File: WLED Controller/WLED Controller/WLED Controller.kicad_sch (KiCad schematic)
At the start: 1 part, among them U1 ESP32-WROOM-32

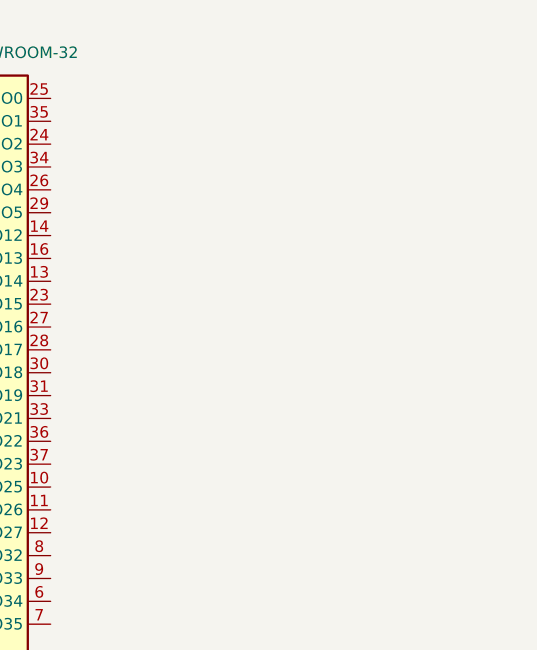
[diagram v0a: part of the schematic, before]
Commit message: Added Level Shifter
SN74AHCT125N
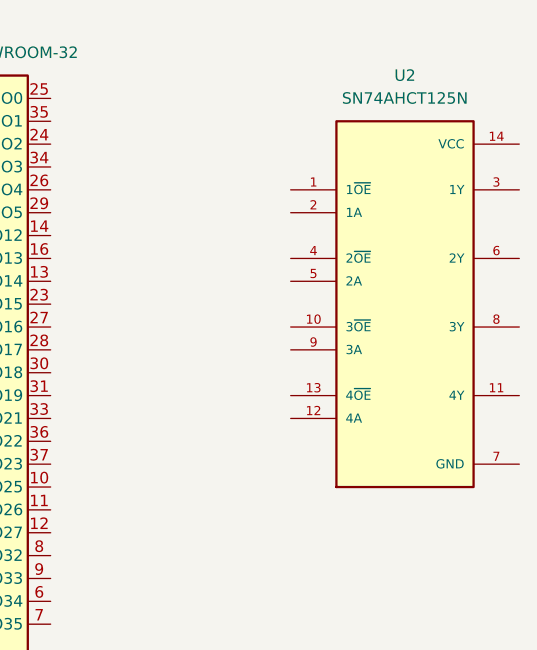
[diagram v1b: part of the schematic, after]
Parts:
- added U2: SN74AHCT125N, Level Shifters:SN74AHCT125N, symbol SN74AHCT125N:SN74AHCT125N
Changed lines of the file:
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@@
+	)
+	(symbol
+		(lib_id "SN74AHCT125N:SN74AHCT125N")
+		(at 166.37 64.77 0)
+		(unit 1)
+		(exclude_from_sim no)
+		(in_bom yes)
+		(on_board yes)
+		(dnp no)
+		(fields_autoplaced yes)
+		(property "Reference" "U2"
+			(at 166.37 39.37 0)
+			(effects
+				(font
+					(size 1.27 1.27)
+				)
+			)
+		)
+		(property "Value" "SN74AHCT125N"
+			(at 166.37 41.91 0)
+			(effects
+				(font
+					(size 1.27 1.27)
+				)
+			)
+		)
+		(property "Footprint" "Level Shifters:SN74AHCT125N"
+			(at 166.37 64.77 0)
+			(effects
+				(font
+					(size 1.27 1.27)
+				)
+				(justify bottom)
+				(hide yes)
+			)
+		)
+		(property "Datasheet" ""
+			(at 166.37 64.77 0)
+			(effects
+				(font
+					(size 1.27 1.27)
+				)
+				(hide yes)
+			)
+		)
+		(property "Description" ""
+			(at 166.37 64.77 0)
+			(effects
+				(font
+					(size 1.27 1.27)
+				)
+				(hide yes)
+			)
+		)
+		(property "PARTREV" "Q"
+			(at 166.37 64.77 0)
+			(effects
+				(font
+					(size 1.27 1.27)
+				)
+				(justify bottom)
+				(hide yes)
+			)
+		)
+		(property "STANDARD" "Manufacturer Recommendations"
+			(at 166.37 64.77 0)
+			(effects
+				(font
+					(size 1.27 1.27)
+				)
+				(justify bottom)
+				(hide yes)
+			)
+		)
+		(property "MAXIMUM_PACKAGE_HEIGHT" "5.08mm"
+			(at 166.37 64.77 0)
+			(effects
+				(font
+					(size 1.27 1.27)
+				)
+				(justify bottom)
+				(hide yes)
+			)
+		)
+		(property "MANUFACTURER" "Texas Instruments"
+			(at 166.37 64.77 0)
+			(effects
+				(font
+					(size 1.27 1.27)
+				)
+				(justify bottom)
+				(hide yes)
+			)
+		)
+		(pin "1"
+		)
+		(pin "5"
+		)
+		(pin "12"
+		)
+		(pin "9"
+		)
+		(pin "8"
+		)
+		(pin "3"
+		)
+		(pin "11"
+		)
+		(pin "7"
+		)
+		(pin "4"
+		)
+		(pin "14"
+		)
+		(pin "13"
+		)
+		(pin "6"
+		)
+		(pin "2"
+		)
+		(pin "10"
+		)
+		(instances
+			(project ""
+				(path "/e8736a94-4ef8-408c-b7cc-dcf1b7df2117"
+					(reference "U2")
+					(unit 1)
+				)
+			)
+		)
 	)
 	(symbol

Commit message: Audio Jack Added
Added Audio Jack
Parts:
- added J1: AudioJack3, Connector_Audio:Jack_3.5mm_CUI_SJ-3523-SMT_Horizontal, symbol Connector_Audio:AudioJack3
- added J2: AudioJack4, Connector_Audio:Jack_3.5mm_PJ320D_Horizontal, symbol Connector_Audio:AudioJack4
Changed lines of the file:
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@@
+	)
+	(symbol
+		(lib_id "Connector_Audio:AudioJack4")
+		(at 218.44 55.88 0)
+		(unit 1)
+		(exclude_from_sim no)
+		(in_bom yes)
+		(on_board yes)
+		(dnp no)
+		(fields_autoplaced yes)
+		(property "Reference" "J2"
+			(at 215.9 46.99 0)
+			(effects
+				(font
+					(size 1.27 1.27)
+				)
+			)
+		)
+		(property "Value" "AudioJack4"
+			(at 215.9 49.53 0)
+			(effects
+				(font
+					(size 1.27 1.27)
+				)
+			)
+		)
+		(property "Footprint" "Connector_Audio:Jack_3.5mm_PJ320D_Horizontal"
+			(at 218.44 55.88 0)
+			(effects
+				(font
+					(size 1.27 1.27)
+				)
+				(hide yes)
+			)
+		)
+		(property "Datasheet" "https://sharvielectronics.com/wp-content/uploads/2021/07/Audio-Jack-3.5mm-TRRS-SMD.pdf"
+			(at 218.44 55.88 0)
+			(effects
+				(font
+					(size 1.27 1.27)
+				)
+				(hide yes)
+			)
+		)
+		(property "Description" "Audio Jack, 4 Poles (TRRS)"
+			(at 218.44 55.88 0)
+			(effects
+				(font
+					(size 1.27 1.27)
+				)
+				(hide yes)
+			)
+		)
+		(pin "S"
+		)
+		(pin "R2"
+		)
+		(pin "R1"
+		)
+		(pin "T"
+		)
+		(instances
+			(project ""
+				(path "/e8736a94-4ef8-408c-b7cc-dcf1b7df2117"
+					(reference "J2")
+					(unit 1)
+				)
+			)
+		)
 	)
 	(symbol
@@
 					(unit 1)
 				)
+			)
+		)
+	)
+	(symbol
+		(lib_id "Connector_Audio:AudioJack3")
+		(at 195.58 55.88 0)
+		(unit 1)
+		(exclude_from_sim no)
+		(in_bom yes)
+		(on_board yes)
+		(dnp no)
+		(fields_autoplaced yes)
+		(property "Reference" "J1"
+			(at 193.675 46.99 0)
+			(effects
+				(font
+					(size 1.27 1.27)
+				)
+			)
+		)
+		(property "Value" "AudioJack3"
+			(at 193.675 49.53 0)
+			(effects
+				(font
+					(size 1.27 1.27)
+				)
+			)
+		)
+		(property "Footprint" "Connector_Audio:Jack_3.5mm_CUI_SJ-3523-SMT_Horizontal"
+			(at 195.58 55.88 0)
+			(effects
+				(font
+					(size 1.27 1.27)
+				)
+				(hide yes)
+			)
+		)
+		(property "Datasheet" "~"
+			(at 195.58 55.88 0)
+			(effects
+				(font
+					(size 1.27 1.27)
+				)
+				(hide yes)
+			)
+		)
+		(property "Description" "Audio Jack, 3 Poles (Stereo / TRS)"
+			(at 195.58 55.88 0)
+			(effects
+				(font
+					(size 1.27 1.27)
+				)
+				(hide yes)
+			)
+		)
+		(pin "R"
+		)
+		(pin "S"
+		)
+		(pin "T"
+		)
+		(instances
+			(project ""
+				(path "/e8736a94-4ef8-408c-b7cc-dcf1b7df2117"
+					(reference "J1")
+					(unit 1)
+				)

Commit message: ADDED
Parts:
- added J3: MIC IN, Connector_PinHeader_2.54mm:PinHeader_1x03_P2.54mm_Vertical, symbol PCM_SL_Pin_Headers:PINHD_1x3_Male
- added J4, J5, J6, J7: PINHD_1x3_Male, Connector_PinHeader_2.54mm:PinHeader_1x03_P2.54mm_Vertical, symbol PCM_SL_Pin_Headers:PINHD_1x3_Male
- added K1: Relay_SPDT, symbol Relay:Relay_SPDT
- added SW1, SW2: SW_Push, symbol Switch:SW_Push
- added U3: AMS1117-3.3, Package_TO_SOT_SMD:SOT-223-3_TabPin2, symbol Regulator_Linear:AMS1117-3.3
- U1: Design Guide (none) -> file:///C:/Users/ARUN/Desktop/COMPS/ESP32-WROOM-32E_V1.2_Re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
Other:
- moved on the sheet: J1, U2

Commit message: NEW
 CHANGES
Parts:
- added D1: WS2812B-2020, LED_SMD:LED_WS2812B-2020_PLCC4_2.0x2.0mm, symbol LED:WS2812B-2020
- J4: value PINHD_1x3_Male -> IR In
- J5: value PINHD_1x3_Male -> ~
- J7: value PINHD_1x3_Male -> Ex Switch in
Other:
- moved on the sheet: K1
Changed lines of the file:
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@@
+	)
+	(symbol
+		(lib_id "LED:WS2812B-2020")
+		(at 247.65 104.14 0)
+		(unit 1)
+		(exclude_from_sim no)
+		(in_bom yes)
+		(on_board yes)
+		(dnp no)
+		(fields_autoplaced yes)
+		(property "Reference" "D1"
+			(at 261.62 97.8214 0)
+			(effects
+				(font
+					(size 1.27 1.27)
+				)
+			)
+		)
+		(property "Value" "WS2812B-2020"
+			(at 261.62 100.3614 0)
+			(effects
+				(font
+					(size 1.27 1.27)
+				)
+			)
+		)
+		(property "Footprint" "LED_SMD:LED_WS2812B-2020_PLCC4_2.0x2.0mm"
+			(at 248.92 111.76 0)
+			(effects
+				(font
+					(size 1.27 1.27)
+				)
+				(justify left top)
+				(hide yes)
+			)
+		)
+		(property "Datasheet" "https://cdn-shop.adafruit.com/product-files/4684/4684_WS2812B-2020_V1.3_EN.pdf"
+			(at 250.19 113.665 0)
+			(effects
+				(font
+					(size 1.27 1.27)
+				)
+				(justify left top)
+				(hide yes)
+			)
+		)
+		(property "Description" "RGB LED with integrated controller, 2.0 x 2.0 mm, 12 mA"
+			(at 247.65 104.14 0)
+			(effects
+				(font
+					(size 1.27 1.27)
+				)
+				(hide yes)
+			)
+		)
+		(pin "3"
+		)
+		(pin "2"
+		)
+		(pin "4"
+		)
+		(pin "1"
+		)
+		(instances
+			(project ""
+				(path "/e8736a94-4ef8-408c-b7cc-dcf1b7df2117"
+					(reference "D1")
+					(unit 1)
+				)
+			)
+		)
 	)
 	(symbol
@@
 			)
 		)
-		(property "Value" "PINHD_1x3_Male"
+		(property "Value" "Ex Switch in"
 			(at 262.89 35.5599 0)
 			(effects
@@
 			)
 		)
-		(property "Value" "PINHD_1x3_Male"
+		(property "Value" "IR In"
 			(at 262.89 26.6699 0)
 			(effects
@@
 	(symbol
 		(lib_id "Relay:Relay_SPDT")
-		(at 181.61 146.05 0)
+		(at 214.63 102.87 0)
 		(unit 1)
 		(exclude_from_sim no)
@@
 		(fields_autoplaced yes)
 		(property "Reference" "K1"
-			(at 193.04 144.7799 0)
+			(at 226.06 101.5999 0)
 			(effects
 				(font
@@
 		)
 		(property "Value" "Relay_SPDT"
-			(at 193.04 147.3199 0)
+			(at 226.06 104.1399 0)
 			(effects
 				(font
@@
 		)
 		(property "Footprint" ""
-			(at 193.04 147.32 0)
+			(at 226.06 104.14 0)
 			(effects
 				(font
@@
 		)
 		(property "Datasheet" "~"
-			(at 181.61 146.05 0)
+			(at 214.63 102.87 0)
 			(effects
 				(font
@@
 		)
 		(property "Description" "Relay SPDT, monostable, EN50005"
-			(at 181.61 146.05 0)
+			(at 214.63 102.87 0)
 			(effects
 				(font
@@
 			)
 		)
-		(property "Value" "PINHD_1x3_Male"
+		(property "Value" "~"
 			(at 262.89 44.4499 0)
 			(effects
